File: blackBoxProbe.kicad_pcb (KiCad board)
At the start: 4 copper layers, 45.5 x 32 mm, 5 parts

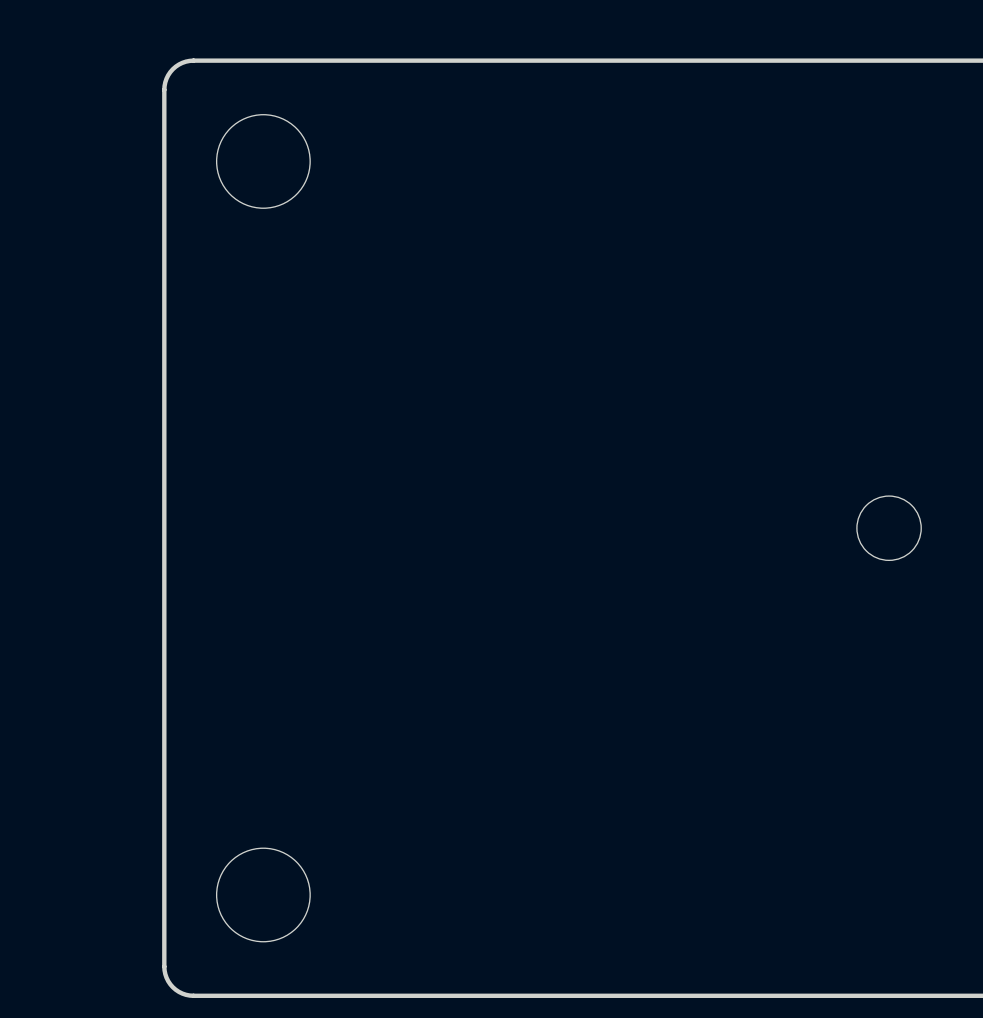
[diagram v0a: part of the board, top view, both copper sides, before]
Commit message: * schematic layout of usb input and powersupply * PCB placing of usb input and powersupply
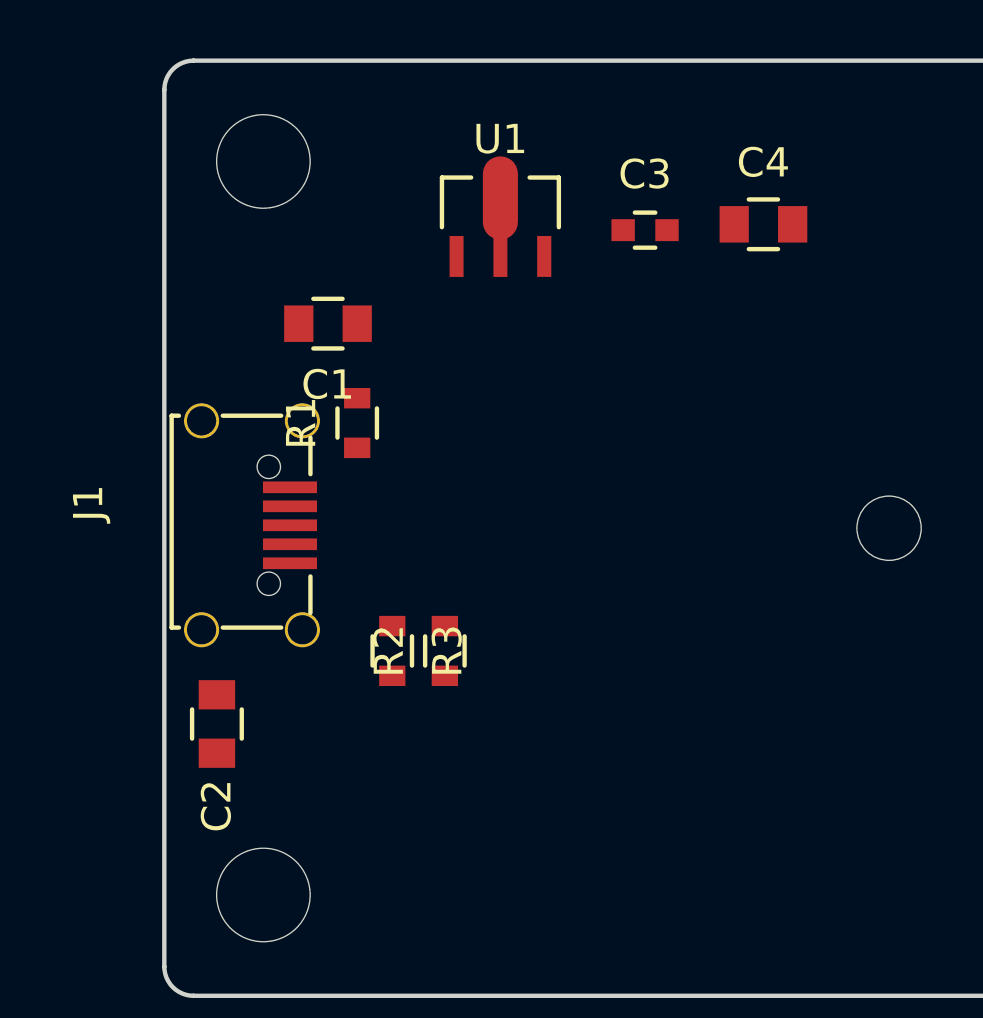
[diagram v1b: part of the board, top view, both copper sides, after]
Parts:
- added C1: 2.2u, SquantorRcl:C_0805, F.Cu at (128.8, 94.1)
- added C2: 100N, SquantorRcl:C_0805, F.Cu at (125.0, 107.8)
- added C3: 100n, SquantorRcl:C_0603, F.Cu at (139.7, 90.9)
- added C4: 10u, SquantorRcl:C_0805, F.Cu at (143.7, 90.7)
- added J1: USB-ID, SquantorUsb:SquantorUsb-USB-UB-SMD4H, F.Cu at (126.2, 101.0)
- added R1: FB, SquantorRcl:R_0603_hand, F.Cu at (129.8, 97.5)
- added R2: R, SquantorRcl:R_0603_hand, F.Cu at (132.8, 105.3)
- added R3: R, SquantorRcl:R_0603_hand, F.Cu at (131.0, 105.3)
- added U1: MCP1702-MB, SquantorMicrochip:MB-(SOT-89), F.Cu at (134.7, 91.8)

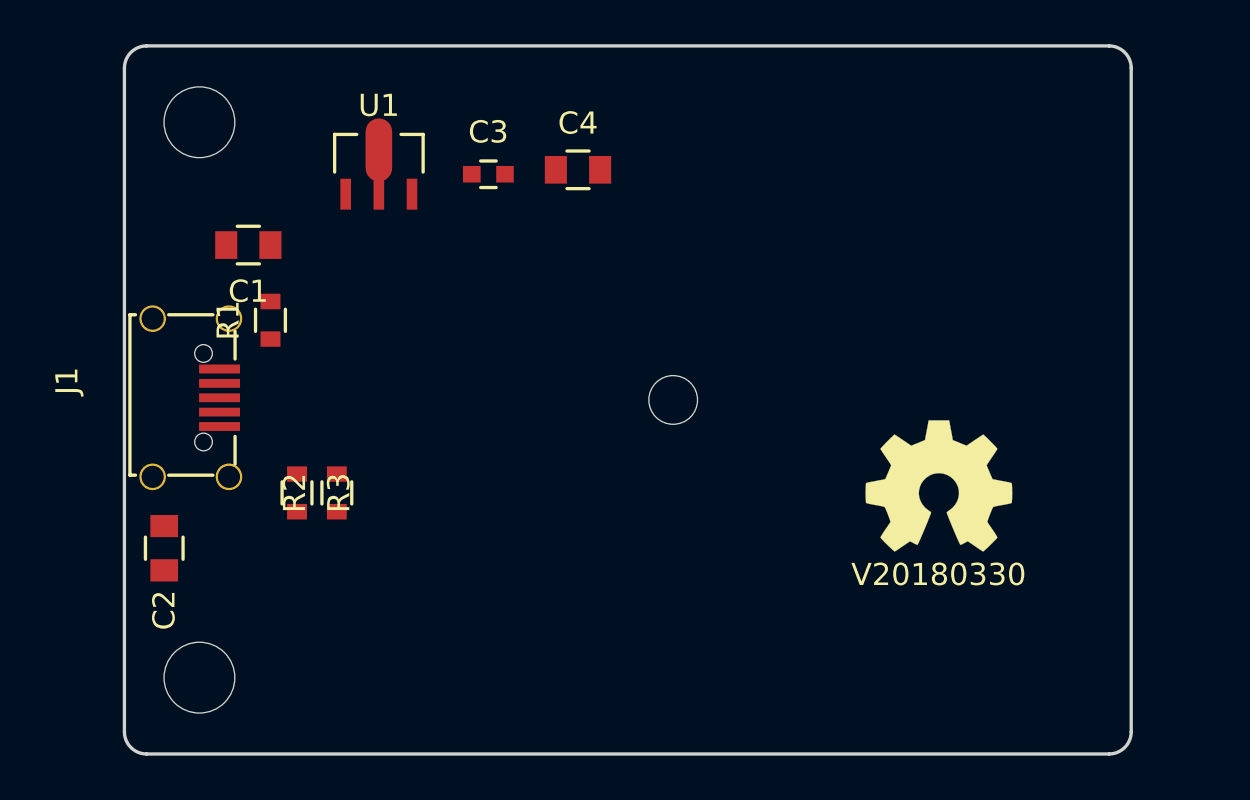
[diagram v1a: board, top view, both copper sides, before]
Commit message: DONE: switched over case to hammond 1551G
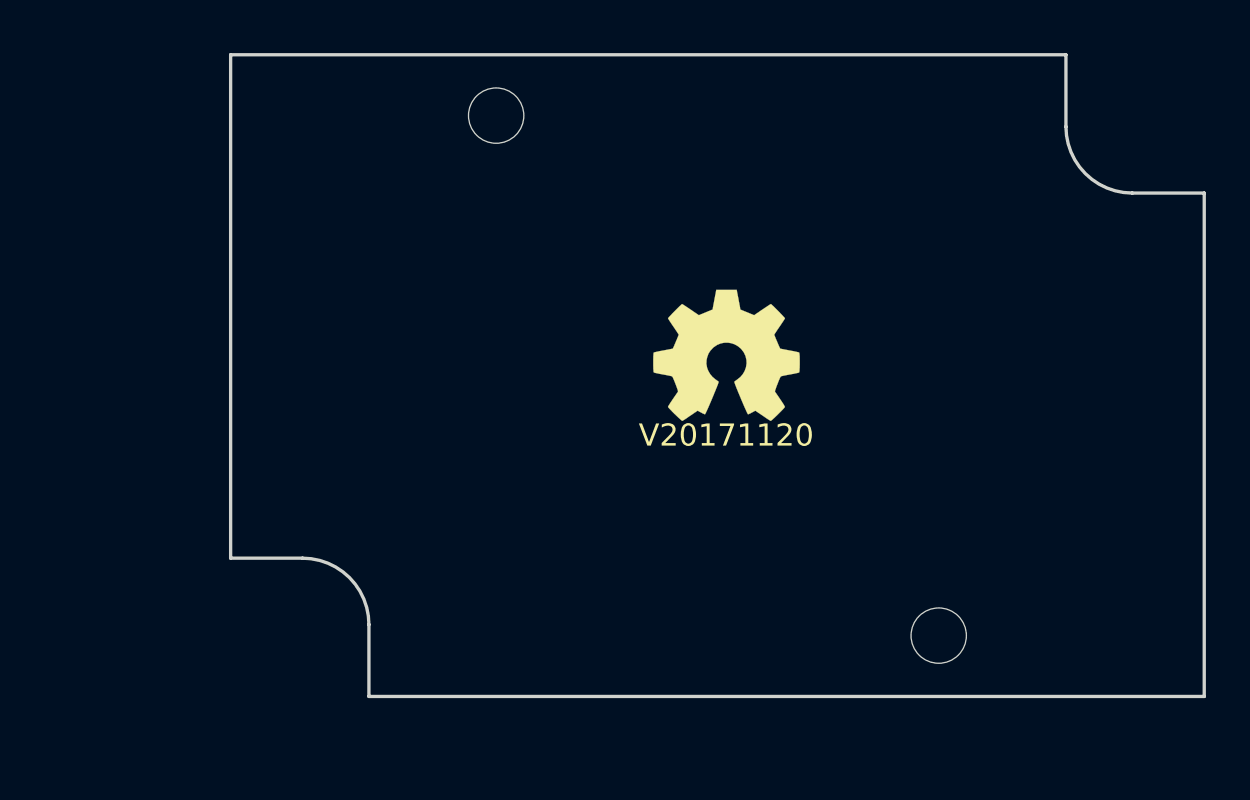
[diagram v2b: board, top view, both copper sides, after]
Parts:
- removed C1: 2.2u, SquantorRcl:C_0805
- removed C2: 100N, SquantorRcl:C_0805
- removed C3: 100n, SquantorRcl:C_0603
- removed C4: 10u, SquantorRcl:C_0805
- removed H3: Drill_Hole_no_metal, SquantorPcbOutline:MountingHole_2.2mm_no_metal
- removed J1: USB-ID, SquantorUsb:SquantorUsb-USB-UB-SMD4H
- removed R1: FB, SquantorRcl:R_0603_hand
- removed R2, R3: R, SquantorRcl:R_0603_hand
- removed U1: MCP1702-MB, SquantorMicrochip:MB-(SOT-89)
- H1, H2: footprint SquantorPcbOutline:MountingHole_3.2mm_no_metal -> SquantorPcbOutline:MountingHole_2.5mm_no_metal
- N2: value V20180330 -> V20171120
- moved H2 40.7 mm to (160.0, 111.8)
- moved H1 28.7 mm to (140.0, 88.2)
- moved N2 11.5 mm to (150.4, 102.7)
- moved N1 11.3 mm to (150.4, 99.1)
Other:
- board size 45.5 x 32 mm -> 44 x 29 mm

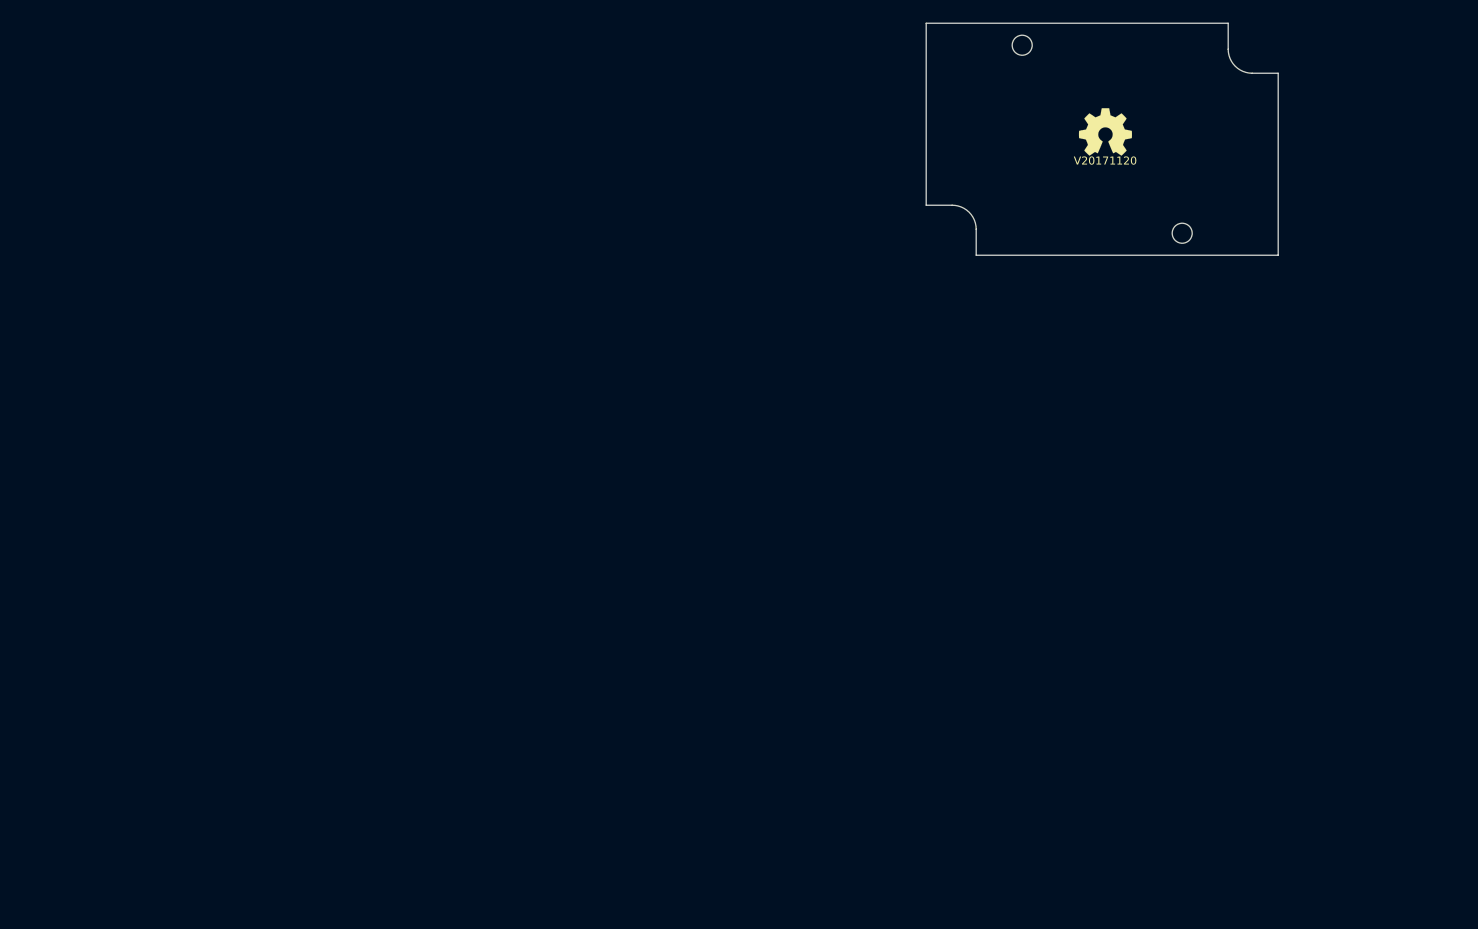
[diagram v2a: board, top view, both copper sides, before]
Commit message: DONE: imported netlist to PCB WIP: initial placing, thinking about replacing all R and C by 0402
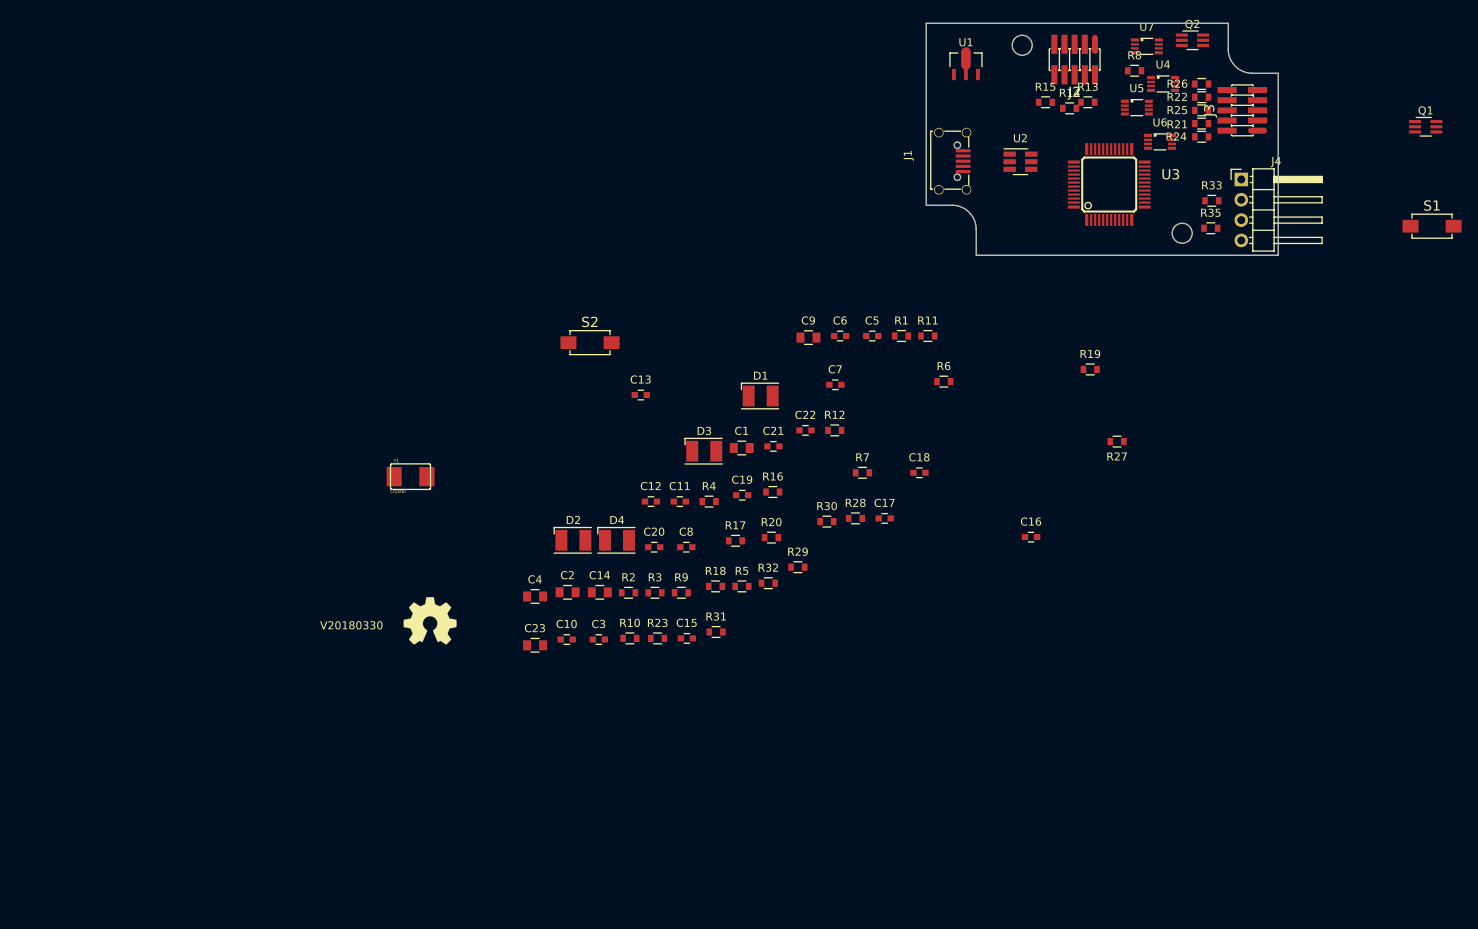
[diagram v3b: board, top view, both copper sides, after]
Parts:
- added C1: 2.2u, SquantorRcl:C_0805, F.Cu at (104.9, 138.6)
- added C10: 100n, SquantorRcl:C_0603, F.Cu at (83.1, 162.5)
- added C11: 100n, SquantorRcl:C_0603, F.Cu at (97.2, 145.3)
- added C12: C, SquantorRcl:C_0603, F.Cu at (93.6, 145.3)
- added C13: C, SquantorRcl:C_0603, F.Cu at (92.3, 132.0)
- added C14: 10u, SquantorRcl:C_0805, F.Cu at (87.2, 156.6)
- added C15: 100n, SquantorRcl:C_0603, F.Cu at (98.1, 162.4)
- added C16: 100n, SquantorRcl:C_0603, F.Cu at (141.1, 149.7)
- added C17: 100n, SquantorRcl:C_0603, F.Cu at (122.8, 147.4)
- added C18: 100n, SquantorRcl:C_0603, F.Cu at (127.2, 141.7)
- added C19: 100n, SquantorRcl:C_0603, F.Cu at (105.0, 144.5)
- added C2: 100N, SquantorRcl:C_0805, F.Cu at (83.2, 156.6)
- added C20: 100n, SquantorRcl:C_0603, F.Cu at (94.0, 151.0)
- added C21: 100n, SquantorRcl:C_0603, F.Cu at (108.9, 138.4)
- added C22: 100n, SquantorRcl:C_0603, F.Cu at (112.9, 136.4)
- added C23: 10u, SquantorRcl:C_0805, F.Cu at (79.1, 163.3)
- added C3: 100n, SquantorRcl:C_0603, F.Cu at (87.1, 162.5)
- added C4: 10u, SquantorRcl:C_0805, F.Cu at (79.1, 157.2)
- added C5: 100n, SquantorRcl:C_0603, F.Cu at (121.3, 124.6)
- added C6: 100n, SquantorRcl:C_0603, F.Cu at (117.2, 124.6)
- added C7: 100n, SquantorRcl:C_0603, F.Cu at (116.6, 130.7)
- added C8: 100n, SquantorRcl:C_0603, F.Cu at (98.0, 151.0)
- added C9: 10u, SquantorRcl:C_0805, F.Cu at (113.3, 124.8)
- added D1: Green, LEDs:LED_PLCC-2, F.Cu at (107.3, 132.1)
- added D2: Yellow, LEDs:LED_PLCC-2, F.Cu at (83.9, 150.1)
- added D3: Orange, LEDs:LED_PLCC-2, F.Cu at (100.3, 139.0)
- added D4: Red, LEDs:LED_PLCC-2, F.Cu at (89.3, 150.1)
- added J1: USB-ID, SquantorUsb:SquantorUsb-USB-UB-SMD4H, F.Cu at (131.3, 102.7)
- added J2: JTAG_2X05, SquantorConnectors:Header-0127-2X05-SMD, F.Cu at (146.6, 90.0)
- added J3: JTAG_2X05, SquantorConnectors:Header-0127-2X05-SMD, F.Cu at (167.5, 96.4)
- added J4: Conn_01x04, Pin_Headers:Pin_Header_Angled_1x04_Pitch2.54mm, F.Cu at (167.4, 105.0)
- added Q1: Q_NMOS_DUAL, TO_SOT_Packages_SMD:SOT-363_SC-70-6_Handsoldering, F.Cu at (190.4, 98.4)
- added Q2: Q_PMOS_DUAL, TO_SOT_Packages_SMD:SOT-363_SC-70-6_Handsoldering, F.Cu at (161.3, 87.6)
- added R1: FB, SquantorRcl:R_0603_hand, F.Cu at (124.9, 124.6)
- added R10: 4.7K, SquantorRcl:R_0603_hand, F.Cu at (91.0, 162.4)
- added R11: 10K, SquantorRcl:R_0603_hand, F.Cu at (128.2, 124.6)
- added R12: 10K, SquantorRcl:R_0603_hand, F.Cu at (116.6, 136.4)
- added R13: 100, SquantorRcl:R_0603_hand, F.Cu at (148.2, 95.4)
- added R14: 100, SquantorRcl:R_0603_hand, F.Cu at (145.9, 96.1)
- added R15: 100, SquantorRcl:R_0603_hand, F.Cu at (142.9, 95.4)
- added R16: 1.5K, SquantorRcl:R_0603_hand, F.Cu at (108.8, 144.1)
- added R17: 10K, SquantorRcl:R_0603_hand, F.Cu at (104.2, 150.2)
- added R18: 47K, SquantorRcl:R_0603_hand, F.Cu at (101.7, 155.9)
- added R19: 10, SquantorRcl:R_0603_hand, F.Cu at (148.5, 128.8)
- added R2: R, SquantorRcl:R_0603_hand, F.Cu at (90.8, 156.7)
- added R20: 10K, SquantorRcl:R_0603_hand, F.Cu at (108.7, 149.8)
- added R21: 100, SquantorRcl:R_0603_hand, F.Cu at (162.4, 98.0)
- added R22: 100, SquantorRcl:R_0603_hand, F.Cu at (162.4, 94.7)
- added R23: 10K, SquantorRcl:R_0603_hand, F.Cu at (94.4, 162.4)
- added R24: 100, SquantorRcl:R_0603_hand, F.Cu at (162.4, 99.7)
- added R25: 100, SquantorRcl:R_0603_hand, F.Cu at (162.4, 96.4)
- added R26: 100, SquantorRcl:R_0603_hand, F.Cu at (162.4, 93.1)
- added R27: 100, SquantorRcl:R_0603_hand, F.Cu at (151.9, 137.8)
- added R28: 10K, SquantorRcl:R_0603_hand, F.Cu at (119.2, 147.4)
- added R29: 330, SquantorRcl:R_0603_hand, F.Cu at (112.0, 153.5)
- added R3: R, SquantorRcl:R_0603_hand, F.Cu at (94.1, 156.7)
- added R30: 330, SquantorRcl:R_0603_hand, F.Cu at (115.6, 147.8)
- added R31: 330, SquantorRcl:R_0603_hand, F.Cu at (101.7, 161.6)
- added R32: 330, SquantorRcl:R_0603_hand, F.Cu at (108.3, 155.5)
- added R33: 100, SquantorRcl:R_0603_hand, F.Cu at (163.7, 107.7)
- added R35: 100, SquantorRcl:R_0603_hand, F.Cu at (163.6, 111.1)
- added R4: R, SquantorRcl:R_0603_hand, F.Cu at (100.9, 145.3)
- added R5: R, SquantorRcl:R_0603_hand, F.Cu at (105.0, 155.9)
- added R6: 10K, SquantorRcl:R_0603_hand, F.Cu at (130.2, 130.3)
- added R7: 4.7K, SquantorRcl:R_0603_hand, F.Cu at (120.0, 141.7)
- added R8: 100, SquantorRcl:R_0603_hand, F.Cu at (154.1, 91.4)
- added R9: 100, SquantorRcl:R_0603_hand, F.Cu at (97.4, 156.7)
- added S1: 2pin_tact_switch, SquantorButtons:DTSM3, F.Cu at (191.2, 110.9)
- added S2: 2pin_tact_switch, SquantorButtons:DTSM3, F.Cu at (86.0, 125.4)
- added U1: MCP1702-MB, SquantorMicrochip:MB-(SOT-89), F.Cu at (133.0, 91.9)
- added U2: USBLC6-2, TO_SOT_Packages_SMD:SOT-23-6_Handsoldering, F.Cu at (139.8, 102.8)
- added U3: STM32F103CBT, SquantorIC:SOT313-2, F.Cu at (150.9, 105.7)
- added U4: 74X2T45, SquantorIC:NXP_SOT765-1_HAND, F.Cu at (157.6, 93.1)
- added U5: 74X2T45, SquantorIC:NXP_SOT765-1_HAND, F.Cu at (154.3, 96.0)
- added U6: 74X2T45, SquantorIC:NXP_SOT765-1_HAND, F.Cu at (157.2, 100.3)
- added U7: 74X2T45, SquantorIC:NXP_SOT765-1_HAND, F.Cu at (155.6, 88.4)
- added Y1: Crystal, SquantorCrystal:SquantorCrystal-CRYSTAL_5.0X3.2, F.Cu at (63.5, 142.2)
- N2: value V20171120 -> V20180330
- moved N2 110.7 mm to (56.2, 160.8)
- moved N1 104.2 mm to (66.0, 160.2)
